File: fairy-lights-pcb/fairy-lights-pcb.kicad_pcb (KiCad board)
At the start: 2 copper layers, 60 x 60 mm, 19 parts, among them J1 Power_Jack, J2 Conn_LED_Strand_SPI, J3 Conn_LED_Strand_WS2812, J4 Conn_I2C, J5 Conn_02x04_Top_Bottom, SW1 SW_PWR, SW2 USER_A, SW3 USER_B, U1 WeMos_D1_mini

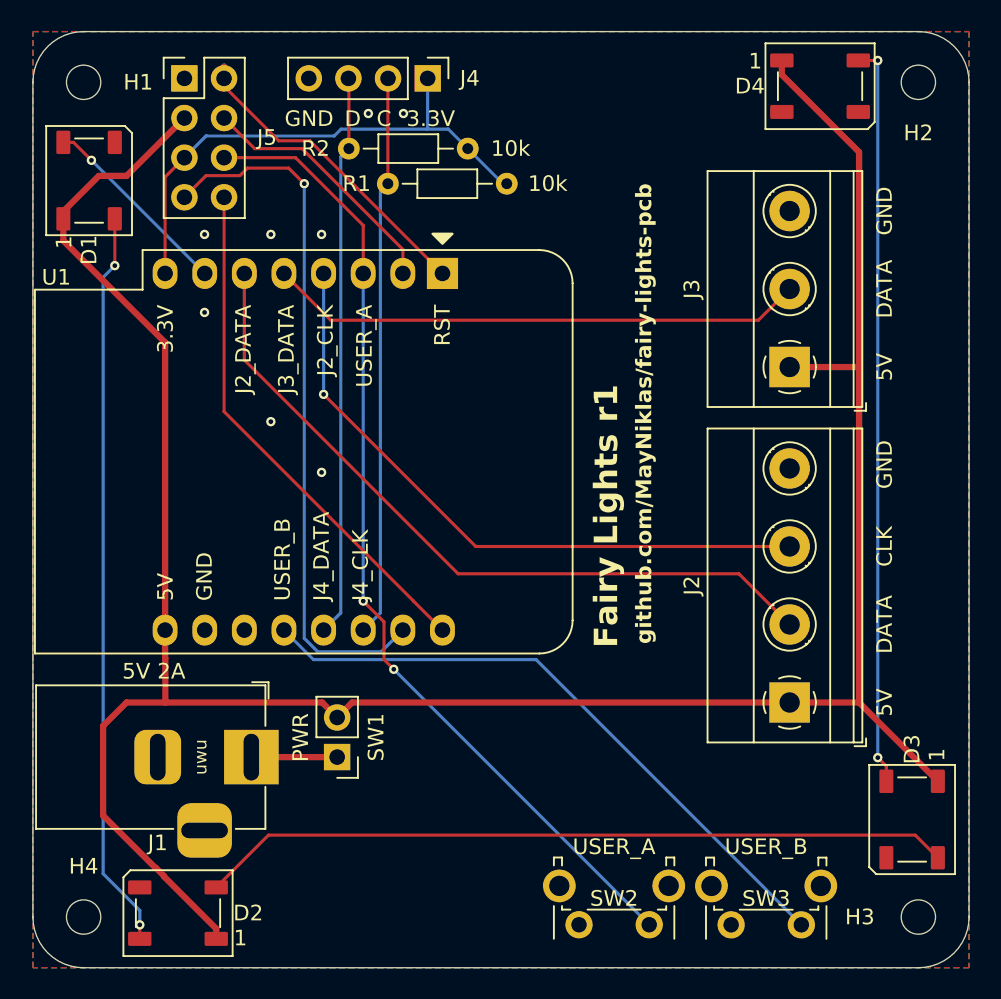
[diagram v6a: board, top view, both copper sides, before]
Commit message: Tweak button pin assignment
Button USER_A is now assigned to pin D3, button USER_B to pin D0.

Since this device is ultimately meant to be mains-powered, deep sleep
support is not a priority (additionally, while the MCU is sleeping,
the LED strand cannot quickly react to external requests delivered via
WiFi). Therefore, now, button USER_A can act as a soft power button (it
can even raise interrupts to wake from light sleep!) and also as a
flashing-mode button, while button USER_B can be used when the board
is fully online.
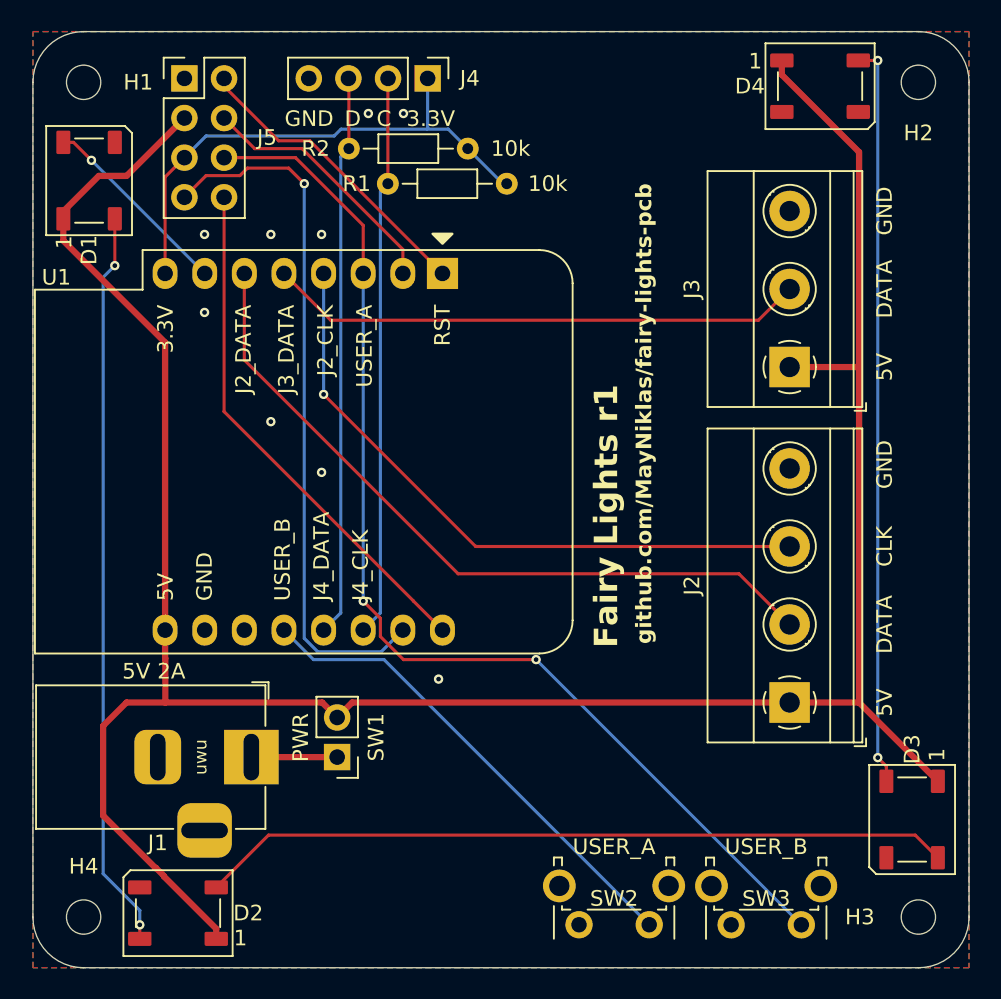
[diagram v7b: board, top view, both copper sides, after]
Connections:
- SW2 pad 1: UC_D0 -> Net-(U1-D3)
- SW3 pad 1: Net-(U1-D3) -> UC_D0
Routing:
- net Net-(U1-D3): track 41.1 -> 31.4 mm
- net UC_D0: track 63.1 -> 72.2 mm
- net UC_RST: track 21.0 -> 19.5 mm
- net GND: vias 8 -> 9
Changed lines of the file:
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@@
 			(layers "*.Cu" "*.Mask")
 			(remove_unused_layers no)
-			(net 13 "UC_D0")
+			(net 14 "Net-(U1-D3)")
 			(pinfunction "1")
 			(pintype "passive")
@@
 			(layers "*.Cu" "*.Mask")
 			(remove_unused_layers no)
-			(net 14 "Net-(U1-D3)")
+			(net 13 "UC_D0")
 			(pinfunction "1")
 			(pintype "passive")
@@
 	)
 	(via
+		(at 86 101.5)
+		(size 0.6)
+		(drill 0.3)
+		(layers "F.Cu" "B.Cu")
+		(free yes)
+		(net 2)
+	)
+	(via
 		(at 75.25 85)
 		(size 0.6)
@@
 	)
 	(segment
-		(start 72.25 63)
-		(end 72.25 62.25)
-		(width 0.4)
-		(layer "F.Cu")
-		(net 10)
-	)
-	(segment
 		(start 75.75 67)
 		(end 72.25 63.5)
@@
 	)
 	(segment
-		(start 72.25 62.24)
-		(end 72.25 63)
-		(width 0.4)
-		(layer "B.Cu")
-		(net 10)
-	)
-	(segment
 		(start 76.3925 68.75)
 		(end 73.75 68.75)
@@
 	)
 	(segment
-		(start 82.5 100.2441)
-		(end 82.5 97.83)
+		(start 82.27 97.6)
+		(end 81.17 96.5)
 		(width 0.2)
 		(layer "F.Cu")
@@
 	)
 	(segment
+		(start 82.27 98.77)
+		(end 82.27 97.6)
+		(width 0.2)
+		(layer "F.Cu")
+		(net 13)
+	)
+	(segment
 		(start 81.17 72.42)
 		(end 76.83 68.08)
@@
 	)
 	(segment
-		(start 82.5 97.83)
-		(end 81.17 96.5)
+		(start 83.75 100.25)
+		(end 82.27 98.77)
 		(width 0.2)
 		(layer "F.Cu")
@@
 	)
 	(segment
-		(start 83.12795 100.87205)
-		(end 82.5 100.2441)
+		(start 92.25 100.25)
+		(end 83.75 100.25)
 		(width 0.2)
 		(layer "F.Cu")
@@
 	)
 	(via
-		(at 83.12795 100.87205)
+		(at 81.17 96.5)
 		(size 0.6)
 		(drill 0.3)
@@
 	)
 	(via
-		(at 81.17 96.5)
+		(at 92.25 100.25)
 		(size 0.6)
 		(drill 0.3)
@@
 	)
 	(segment
-		(start 83.12795 100.87205)
-		(end 99.5 117.2441)
+		(start 92.25 100.25)
+		(end 109.25 117.25)
 		(width 0.2)
 		(layer "B.Cu")
@@
 	)
 	(segment
-		(start 109.25 117.25)
-		(end 92.25 100.25)
+		(start 82.5059 100.25)
+		(end 77.98 100.25)
 		(width 0.2)
 		(layer "B.Cu")
@@
 	)
 	(segment
-		(start 92.25 100.25)
-		(end 77.98 100.25)
+		(start 99.5 117.2441)
+		(end 82.5059 100.25)
 		(width 0.2)
 		(layer "B.Cu")
